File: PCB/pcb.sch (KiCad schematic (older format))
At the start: 14 parts

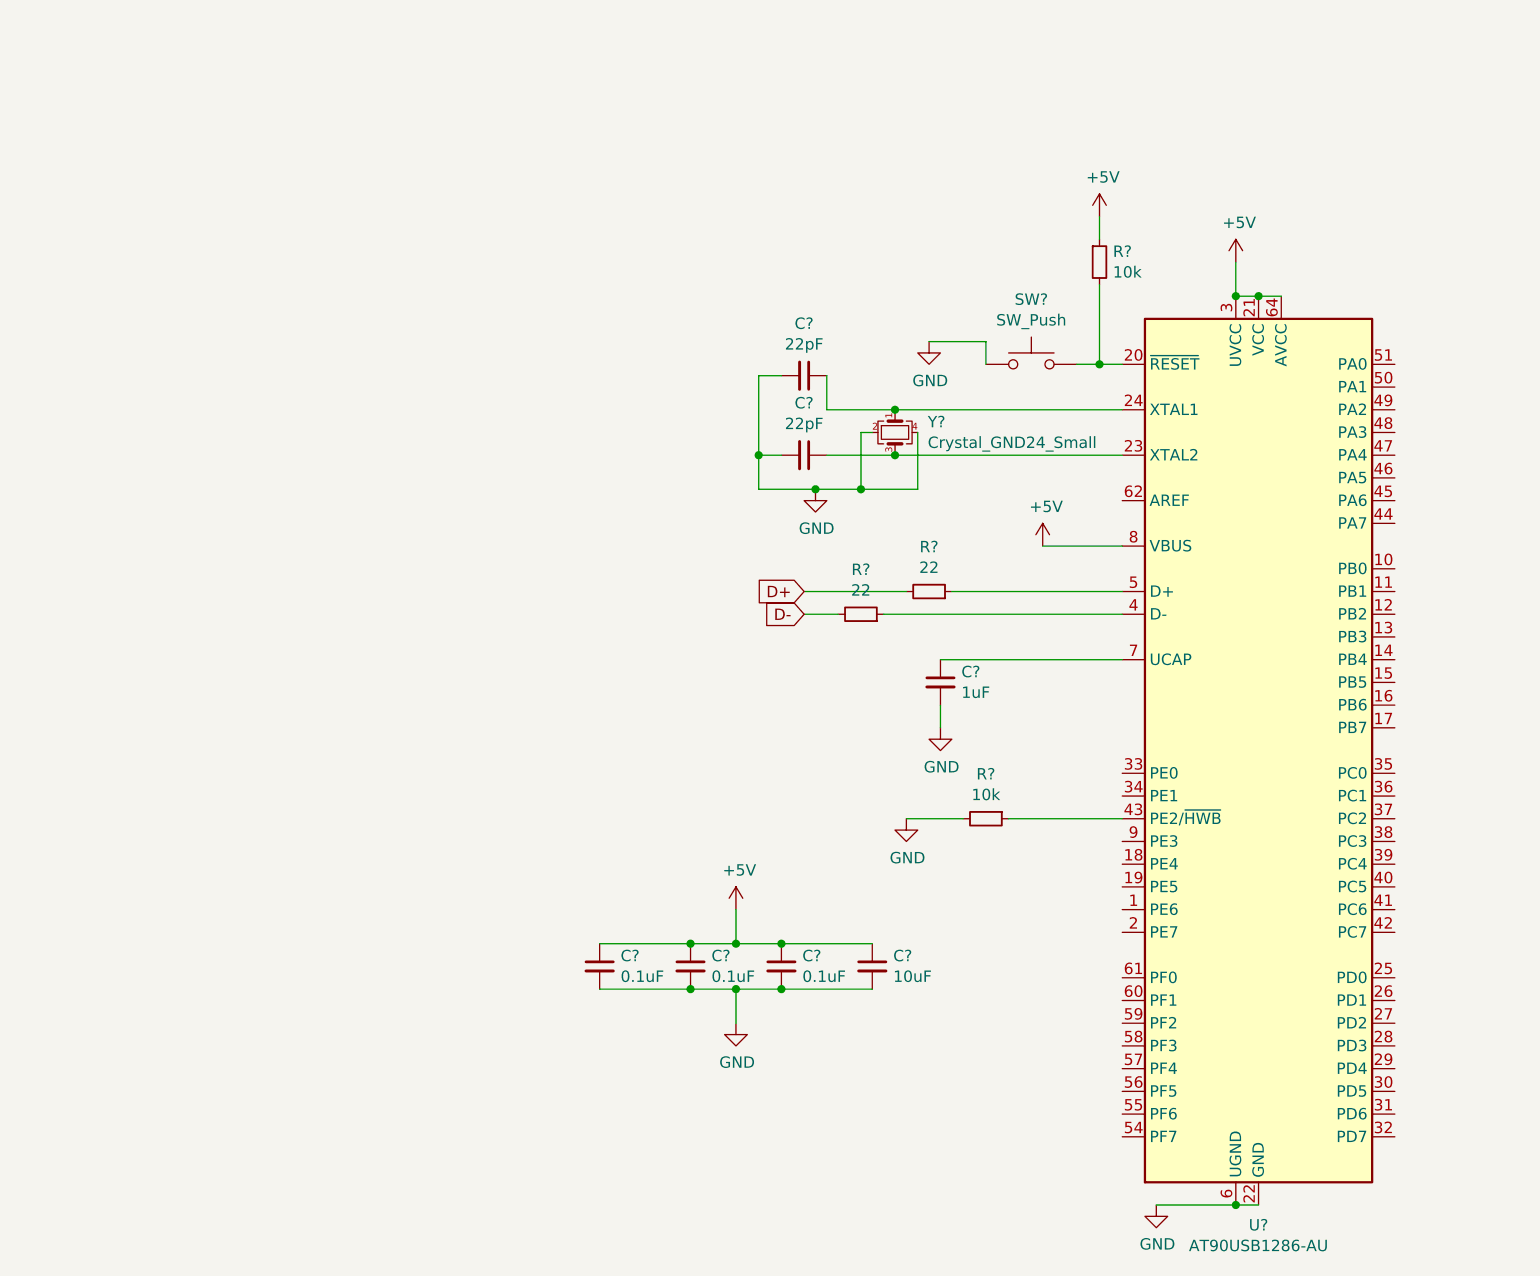
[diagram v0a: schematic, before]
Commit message: USB Circuit added
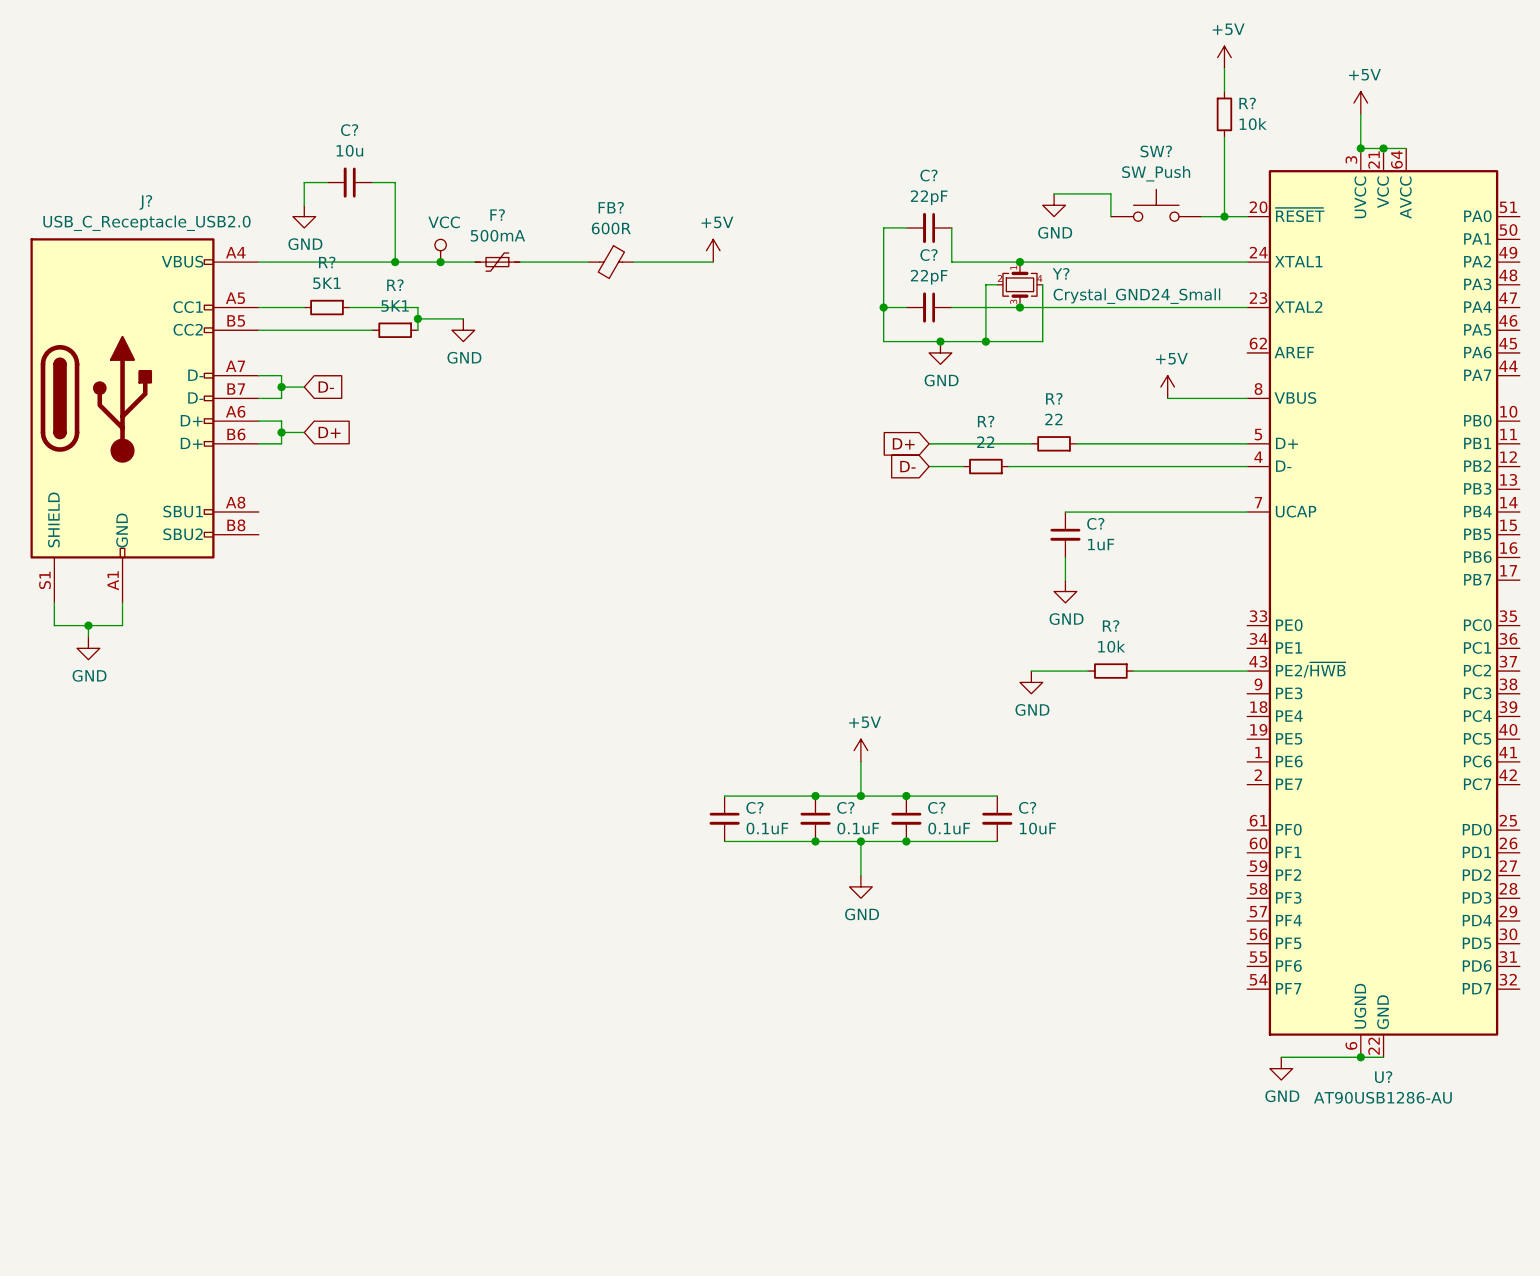
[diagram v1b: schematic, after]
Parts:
- added C?: 10u, symbol Device:C_Small
- added F?: 500mA, symbol Device:Polyfuse_Small
- added FB?: 600R, symbol Device:Ferrite_Bead_Small
- added J?: USB_C_Receptacle_USB2.0, symbol Connector:USB_C_Receptacle_USB2.0
- added R? (x2): 5K1, symbol Device:R_Small
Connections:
- net +5V: now also FB?.1
- net D+: now also J?.A6 (D+), J?.B6 (D+)
- net D-: now also J?.A7 (D-), J?.B7 (D-)
- net GND: now also C?.2, J?.A1 (GND), J?.A12 (GND), J?.B1 (GND), J?.B12 (GND), J?.S1 (SHIELD), R?.1, R?.1
- new net: J?.A5 (CC1), R?.2
- new net: J?.B5 (CC2), R?.2
- new net: F?.1, FB?.2
- new net VCC: C?.1, F?.2, J?.A4 (VBUS), J?.A9 (VBUS), J?.B4 (VBUS), J?.B9 (VBUS)
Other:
- moved on the sheet: C?, R?, SW?, U?, Y?

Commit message: Finished Matrix
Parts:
- added D?: ^, symbol Device:D_Small
- added D? (x2): 1, symbol Device:D_Small
- added D?: Tab, symbol Device:D_Small
- added D?: Q, symbol Device:D_Small
- added D?: Esc, symbol Device:D_Small
- added D?: Caps, symbol Device:D_Small
- added D? (x2): Shift, symbol Device:D_Small
- added D?: Ctrl, symbol Device:D_Small
- added D?: A, symbol Device:D_Small
- added D?: <, symbol Device:D_Small
- added D? (x2): Win, symbol Device:D_Small
- added D? (x2): 2, symbol Device:D_Small
- added D? (x2): 3, symbol Device:D_Small
- added D?: W, symbol Device:D_Small
- added D?: E, symbol Device:D_Small
- added D?: S, symbol Device:D_Small
- added D?: Y, symbol Device:D_Small
- added D?: Alt, symbol Device:D_Small
- added D?: D, symbol Device:D_Small
- added D?: X, symbol Device:D_Small
- added D? (x2): 4, symbol Device:D_Small
- added D? (x2): 5, symbol Device:D_Small
- added D?: R, symbol Device:D_Small
- added D?: T, symbol Device:D_Small
- added D?: F, symbol Device:D_Small
- added D?: C, symbol Device:D_Small
- added D?: G, symbol Device:D_Small
- added D?: V, symbol Device:D_Small
- added D? (x2): 6, symbol Device:D_Small
- added D? (x2): 7, symbol Device:D_Small
- added D?: Z, symbol Device:D_Small
- added D?: U, symbol Device:D_Small
- added D?: H, symbol Device:D_Small
- added D?: B, symbol Device:D_Small
- added D?: J, symbol Device:D_Small
- added D?: N, symbol Device:D_Small
- added D? (x2): 8, symbol Device:D_Small
- added D? (x2): 9, symbol Device:D_Small
- added D?: I, symbol Device:D_Small
- added D?: O, symbol Device:D_Small
- added D?: K, symbol Device:D_Small
- added D?: M, symbol Device:D_Small
- added D?: L, symbol Device:D_Small
- added D? (x2): ,, symbol Device:D_Small
- added D? (x2): 0, symbol Device:D_Small
- added D?: ß, symbol Device:D_Small
- added D?: P, symbol Device:D_Small
- added D?: Ü, symbol Device:D_Small
- added D?: Ö, symbol Device:D_Small
- added D?: ., symbol Device:D_Small
- added D?: Ä, symbol Device:D_Small
- added D? (x2): -, symbol Device:D_Small
- added D?: ´, symbol Device:D_Small
- added D?: Back, symbol Device:D_Small
- added D? (x2): +, symbol Device:D_Small
- added D? (x2): Enter, symbol Device:D_Small
- added D?: #, symbol Device:D_Small
- added D?: Right, symbol Device:D_Small
- added D?: Left, symbol Device:D_Small
- added D?: Up, symbol Device:D_Small
- added D?: Down, symbol Device:D_Small
- added D?: F1, symbol Device:D_Small
- added D?: F2, symbol Device:D_Small
- added D?: F3, symbol Device:D_Small
- added D?: F4, symbol Device:D_Small
- added D?: F5, symbol Device:D_Small
- added D?: F6, symbol Device:D_Small
- added D?: F7, symbol Device:D_Small
- added D?: F8, symbol Device:D_Small
- added D?: F9, symbol Device:D_Small
- added D?: F10, symbol Device:D_Small
- added D?: F11, symbol Device:D_Small
- added D?: F12, symbol Device:D_Small
- added D?: Leer, symbol Device:D_Small
- added D?: AltGr, symbol Device:D_Small
- added D?: Fn, symbol Device:D_Small
- added D?: Insert, symbol Device:D_Small
- added D?: Del, symbol Device:D_Small
- added D?: PgUp, symbol Device:D_Small
- added D?: PgDn, symbol Device:D_Small
- added D?: Druck, symbol Device:D_Small
- added D?: NumLock, symbol Device:D_Small
- added D?: /, symbol Device:D_Small
- added D?: *, symbol Device:D_Small
- added MX? (x100): MX-LED, symbol MX_Alps_Hybrid:MX-LED
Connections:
- new net: D?.2 (A), MX?.2 (ROW) (x100)
- new net COL0: MX?.1 (COL), MX?.1 (COL), MX?.1 (COL), MX?.1 (COL), MX?.1 (COL), MX?.1 (COL)
- new net COL1: MX?.1 (COL), MX?.1 (COL), MX?.1 (COL), MX?.1 (COL), MX?.1 (COL)
- new net COL10: MX?.1 (COL), MX?.1 (COL), MX?.1 (COL), MX?.1 (COL), MX?.1 (COL), MX?.1 (COL)
- new net COL11: MX?.1 (COL), MX?.1 (COL), MX?.1 (COL), MX?.1 (COL), MX?.1 (COL), MX?.1 (COL)
- new net COL12: MX?.1 (COL), MX?.1 (COL), MX?.1 (COL), MX?.1 (COL), MX?.1 (COL), MX?.1 (COL)
- new net COL13: MX?.1 (COL), MX?.1 (COL), MX?.1 (COL), MX?.1 (COL), MX?.1 (COL)
- new net COL14: MX?.1 (COL), MX?.1 (COL), MX?.1 (COL), MX?.1 (COL), MX?.1 (COL), MX?.1 (COL)
- new net COL15: MX?.1 (COL), MX?.1 (COL), MX?.1 (COL), MX?.1 (COL), MX?.1 (COL)
- new net COL16: MX?.1 (COL), MX?.1 (COL), MX?.1 (COL), MX?.1 (COL), MX?.1 (COL), MX?.1 (COL)
- new net COL17: MX?.1 (COL), MX?.1 (COL), MX?.1 (COL)
- new net COL2: MX?.1 (COL), MX?.1 (COL), MX?.1 (COL), MX?.1 (COL), MX?.1 (COL), MX?.1 (COL)
- new net COL3: MX?.1 (COL), MX?.1 (COL), MX?.1 (COL), MX?.1 (COL), MX?.1 (COL)
- new net COL4: MX?.1 (COL), MX?.1 (COL), MX?.1 (COL), MX?.1 (COL), MX?.1 (COL)
- new net COL5: MX?.1 (COL), MX?.1 (COL), MX?.1 (COL), MX?.1 (COL), MX?.1 (COL), MX?.1 (COL)
- new net COL6: MX?.1 (COL), MX?.1 (COL), MX?.1 (COL), MX?.1 (COL), MX?.1 (COL), MX?.1 (COL)
- new net COL7: MX?.1 (COL), MX?.1 (COL), MX?.1 (COL), MX?.1 (COL), MX?.1 (COL), MX?.1 (COL)
- new net COL8: MX?.1 (COL), MX?.1 (COL), MX?.1 (COL), MX?.1 (COL), MX?.1 (COL), MX?.1 (COL)
- new net COL9: MX?.1 (COL), MX?.1 (COL), MX?.1 (COL), MX?.1 (COL), MX?.1 (COL)
- new net ROW0: D?.1 (K), D?.1 (K), D?.1 (K), D?.1 (K), D?.1 (K), D?.1 (K), D?.1 (K), D?.1 (K), D?.1 (K), D?.1 (K), D?.1 (K), D?.1 (K), D?.1 (K), D?.1 (K), D?.1 (K), D?.1 (K)
- new net ROW1: D?.1 (K), D?.1 (K), D?.1 (K), D?.1 (K), D?.1 (K), D?.1 (K), D?.1 (K), D?.1 (K), D?.1 (K), D?.1 (K), D?.1 (K), D?.1 (K), D?.1 (K), D?.1 (K), D?.1 (K), D?.1 (K), D?.1 (K)
- new net ROW2: D?.1 (K), D?.1 (K), D?.1 (K), D?.1 (K), D?.1 (K), D?.1 (K), D?.1 (K), D?.1 (K), D?.1 (K), D?.1 (K), D?.1 (K), D?.1 (K), D?.1 (K), D?.1 (K), D?.1 (K), D?.1 (K), D?.1 (K)
- new net ROW3: D?.1 (K), D?.1 (K), D?.1 (K), D?.1 (K), D?.1 (K), D?.1 (K), D?.1 (K), D?.1 (K), D?.1 (K), D?.1 (K), D?.1 (K), D?.1 (K), D?.1 (K), D?.1 (K), D?.1 (K), D?.1 (K), D?.1 (K)
- new net ROW4: D?.1 (K), D?.1 (K), D?.1 (K), D?.1 (K), D?.1 (K), D?.1 (K), D?.1 (K), D?.1 (K), D?.1 (K), D?.1 (K), D?.1 (K), D?.1 (K), D?.1 (K), D?.1 (K), D?.1 (K), D?.1 (K), D?.1 (K)
- new net ROW5: D?.1 (K), D?.1 (K), D?.1 (K), D?.1 (K), D?.1 (K), D?.1 (K), D?.1 (K), D?.1 (K), D?.1 (K), D?.1 (K), D?.1 (K), D?.1 (K), D?.1 (K), D?.1 (K), D?.1 (K), D?.1 (K)

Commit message: Renamed Switches
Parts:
- gave numbers to parts that had none: 93

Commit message: Added Footprints
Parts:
- C1, C2, C3, C4, C5, C6, C7, C8: renamed from C?; footprint (none) -> Capacitor_SMD:C_0805_2012Metric
- D1, D10, D100, D11, D12, D13, D14, D15, D16, D17, D18, D19, D2, D20, D21, D22, D23, D24, D25, D26, D27, D28, D29, D3, D30, D31, D32, D33, D34, D35, D36, D37, D38, D39, D4, D40, D41, D42, D43, D44, D45, D46, D47, D48, D49, D5, D50, D51, D52, D53, D54, D55, D56, D57, D58, D59, D6, D60, D61, D62, D63, D64, D65, D66, D67, D68, D69, D7, D70, D71, D72, D73, D74, D75, D76, D77, D78, D79, D8, D80, D81, D82, D83, D84, D85, D86, D87, D88, D89, D9, D90, D91, D92, D93, D94, D95, D96, D97, D98, D99: renamed from D?; footprint (none) -> Diode_SMD:D_SOD-123
- F1: renamed from F?; footprint (none) -> Fuse:Fuse_1206_3216Metric
- FB1: renamed from FB?; footprint (none) -> Ferrite_THT:LairdTech_28C0236-0JW-10
- J1: renamed from J?; footprint (none) -> Connector_USB:USB_C_Receptacle_HRO_TYPE-C-31-M-12
- MX*1: renamed from MX*; footprint (none) -> MX_Alps_Hybrid:MX-1U
- MX+1: renamed from MX+; footprint (none) -> MX_Alps_Hybrid:MX-1U
- MX+2: renamed from MX+num; footprint (none) -> MX_Alps_Hybrid:MX-1U
- MX,1: renamed from MX,; footprint (none) -> MX_Alps_Hybrid:MX-1U
- MX,2: renamed from MX,num; footprint (none) -> MX_Alps_Hybrid:MX-1U
- MX-1: renamed from MX-; footprint (none) -> MX_Alps_Hybrid:MX-1U
- MX-2: renamed from MX-num; footprint (none) -> MX_Alps_Hybrid:MX-1U
- MX.1: renamed from MX.; footprint (none) -> MX_Alps_Hybrid:MX-1U
- MX/1: renamed from MX/; footprint (none) -> MX_Alps_Hybrid:MX-1U
- MX0, MX1, MX2, MX3, MX4, MX5, MX6, MX7, MX8, MX9, MXf1, MXf10, MXf11, MXf12, MXf2, MXf3, MXf4, MXf5, MXf6, MXf7, MXf8, MXf9: footprint (none) -> MX_Alps_Hybrid:MX-1U
- MX10: renamed from MXß; footprint (none) -> MX_Alps_Hybrid:MX-1U
- MX11: renamed from MX´; footprint (none) -> MX_Alps_Hybrid:MX-1U
- MX13, MX15, MX16, MX17: renamed from MX?; footprint (none) -> MX_Alps_Hybrid:MX-1U
- MX14: renamed from MXü; footprint (none) -> MX_Alps_Hybrid:MX-1U
- MX^1: renamed from MX^; footprint (none) -> MX_Alps_Hybrid:MX-1U
- MXa1: renamed from MXa; footprint (none) -> MX_Alps_Hybrid:MX-1U
- MXalt1: renamed from MXalt; footprint (none) -> MX_Alps_Hybrid:MX-1U
- MXaltgr1: renamed from MXaltgr; footprint (none) -> MX_Alps_Hybrid:MX-1U
- MXb1: renamed from MXb; footprint (none) -> MX_Alps_Hybrid:MX-1U
- MXback1: renamed from MXback; footprint (none) -> MX_Alps_Hybrid:MX-1U
- MXc1: renamed from MXc; footprint (none) -> MX_Alps_Hybrid:MX-1U
- MXcaps1: renamed from MXcaps; footprint (none) -> MX_Alps_Hybrid:MX-1U
- MXctrl1: renamed from MXctrl; footprint (none) -> MX_Alps_Hybrid:MX-1U
- MXd1: renamed from MXd; footprint (none) -> MX_Alps_Hybrid:MX-1U
- MXdel1: renamed from MXdel; footprint (none) -> MX_Alps_Hybrid:MX-1U
- MXdown1: renamed from MXdown; footprint (none) -> MX_Alps_Hybrid:MX-1U
- MXdruck1: renamed from MXdruck; footprint (none) -> MX_Alps_Hybrid:MX-1U
- MXe1: renamed from MXe; footprint (none) -> MX_Alps_Hybrid:MX-1U
- MXenter1: renamed from MXenternum; footprint (none) -> MX_Alps_Hybrid:MX-1U
- MXesc1: renamed from MXesc; footprint (none) -> MX_Alps_Hybrid:MX-1U
- MXf0: renamed from MXf; footprint (none) -> MX_Alps_Hybrid:MX-1U
- MXfn1: renamed from MXfn; footprint (none) -> MX_Alps_Hybrid:MX-1U
- MXg1: renamed from MXg; footprint (none) -> MX_Alps_Hybrid:MX-1U
- MXh1: renamed from MXh; footprint (none) -> MX_Alps_Hybrid:MX-1U
- MXi1: renamed from MXi; footprint (none) -> MX_Alps_Hybrid:MX-1U
- MXinsert1: renamed from MXinsert; footprint (none) -> MX_Alps_Hybrid:MX-1U
- MXj1: renamed from MXj; footprint (none) -> MX_Alps_Hybrid:MX-1U
- MXk1: renamed from MXk; footprint (none) -> MX_Alps_Hybrid:MX-1U
- MXl1: renamed from MXl; footprint (none) -> MX_Alps_Hybrid:MX-1U
- MXleer1: renamed from MXleer; footprint (none) -> MX_Alps_Hybrid:MX-1U
- MXleft1: renamed from MXleft; footprint (none) -> MX_Alps_Hybrid:MX-1U
- MXm1: renamed from MXm; footprint (none) -> MX_Alps_Hybrid:MX-1U
- MXn1: renamed from MXn; footprint (none) -> MX_Alps_Hybrid:MX-1U
- MXnum0: renamed from MX0num; footprint (none) -> MX_Alps_Hybrid:MX-1U
- MXnum1: renamed from MX1num; footprint (none) -> MX_Alps_Hybrid:MX-1U
- MXnum2: renamed from MX2num; footprint (none) -> MX_Alps_Hybrid:MX-1U
- MXnum3: renamed from MX3num; footprint (none) -> MX_Alps_Hybrid:MX-1U
- MXnum4: renamed from MX4num; footprint (none) -> MX_Alps_Hybrid:MX-1U
- MXnum5: renamed from MX5num; footprint (none) -> MX_Alps_Hybrid:MX-1U
- MXnum6: renamed from MX6num; footprint (none) -> MX_Alps_Hybrid:MX-1U
- MXnum7: renamed from MX7num; footprint (none) -> MX_Alps_Hybrid:MX-1U
- MXnum8: renamed from MX8num; footprint (none) -> MX_Alps_Hybrid:MX-1U
- MXnum9: renamed from MX9num; footprint (none) -> MX_Alps_Hybrid:MX-1U
- MXnumlock1: renamed from MXnumlock; footprint (none) -> MX_Alps_Hybrid:MX-1U
- MXo1: renamed from MXo; footprint (none) -> MX_Alps_Hybrid:MX-1U
- MXp1: renamed from MXp; footprint (none) -> MX_Alps_Hybrid:MX-1U
- MXpgdn1: renamed from MXpgdn; footprint (none) -> MX_Alps_Hybrid:MX-1U
- MXpgup1: renamed from MXpgup; footprint (none) -> MX_Alps_Hybrid:MX-1U
- MXq1: renamed from MXq; footprint (none) -> MX_Alps_Hybrid:MX-1U
- MXr1: renamed from MXr; footprint (none) -> MX_Alps_Hybrid:MX-1U
- MXright1: renamed from MXright; footprint (none) -> MX_Alps_Hybrid:MX-1U
- MXs1: renamed from MXs; footprint (none) -> MX_Alps_Hybrid:MX-1U
- MXshift1, MXshift2: renamed from MXshift; footprint (none) -> MX_Alps_Hybrid:MX-1U
- MXt1: renamed from MXt; footprint (none) -> MX_Alps_Hybrid:MX-1U
- MXtab1: renamed from MXtab; footprint (none) -> MX_Alps_Hybrid:MX-1U
- MXu1: renamed from MXu; footprint (none) -> MX_Alps_Hybrid:MX-1U
- MXup1: renamed from MXup; footprint (none) -> MX_Alps_Hybrid:MX-1U
- MXv1, MXv2: renamed from MXv; footprint (none) -> MX_Alps_Hybrid:MX-1U
- MXw1: renamed from MXw; footprint (none) -> MX_Alps_Hybrid:MX-1U
- MXwin1, MXwin2: renamed from MXwin; footprint (none) -> MX_Alps_Hybrid:MX-1U
- MXx1: renamed from MXx; footprint (none) -> MX_Alps_Hybrid:MX-1U
- MXy1: renamed from MXy; footprint (none) -> MX_Alps_Hybrid:MX-1U
- MXz1: renamed from MXz; footprint (none) -> MX_Alps_Hybrid:MX-1U
- R1, R2, R3, R4, R5, R6: renamed from R?; footprint (none) -> Resistor_SMD:R_0805_2012Metric
- SW1: renamed from SW?; footprint (none) -> random-keyboard-parts:SKQG-1155865
- Y1: renamed from Y?; footprint (none) -> Crystal:Crystal_SMD_3225-4Pin_3.2x2.5mm
- gave numbers to parts that had none: 1
